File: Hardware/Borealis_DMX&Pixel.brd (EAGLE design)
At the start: 62.5 x 28.3 mm, 9 parts, among them IC2 SP3485, J1 RJ45-854602-908LF

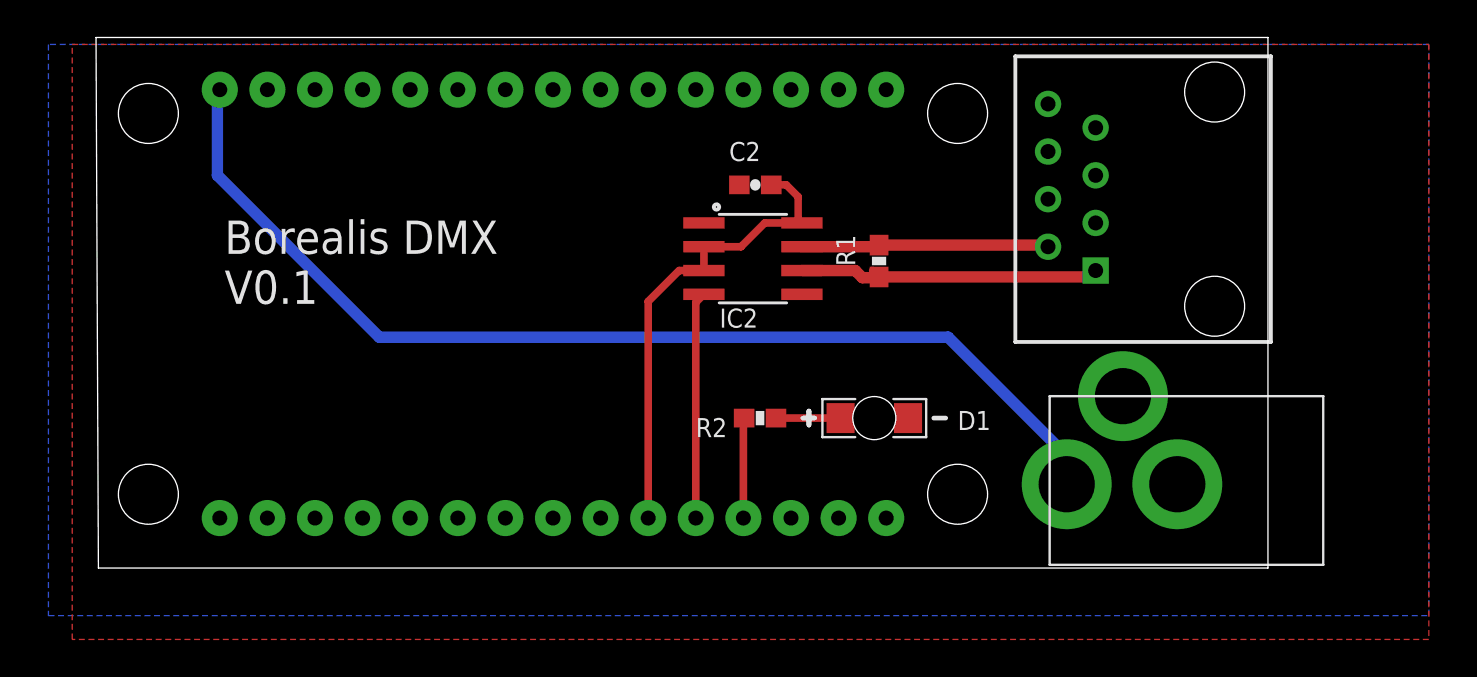
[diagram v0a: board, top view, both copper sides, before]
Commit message: Replaced erroneously committed DMX only output design files with DMX & Pixel version refrenced in repo documentation.
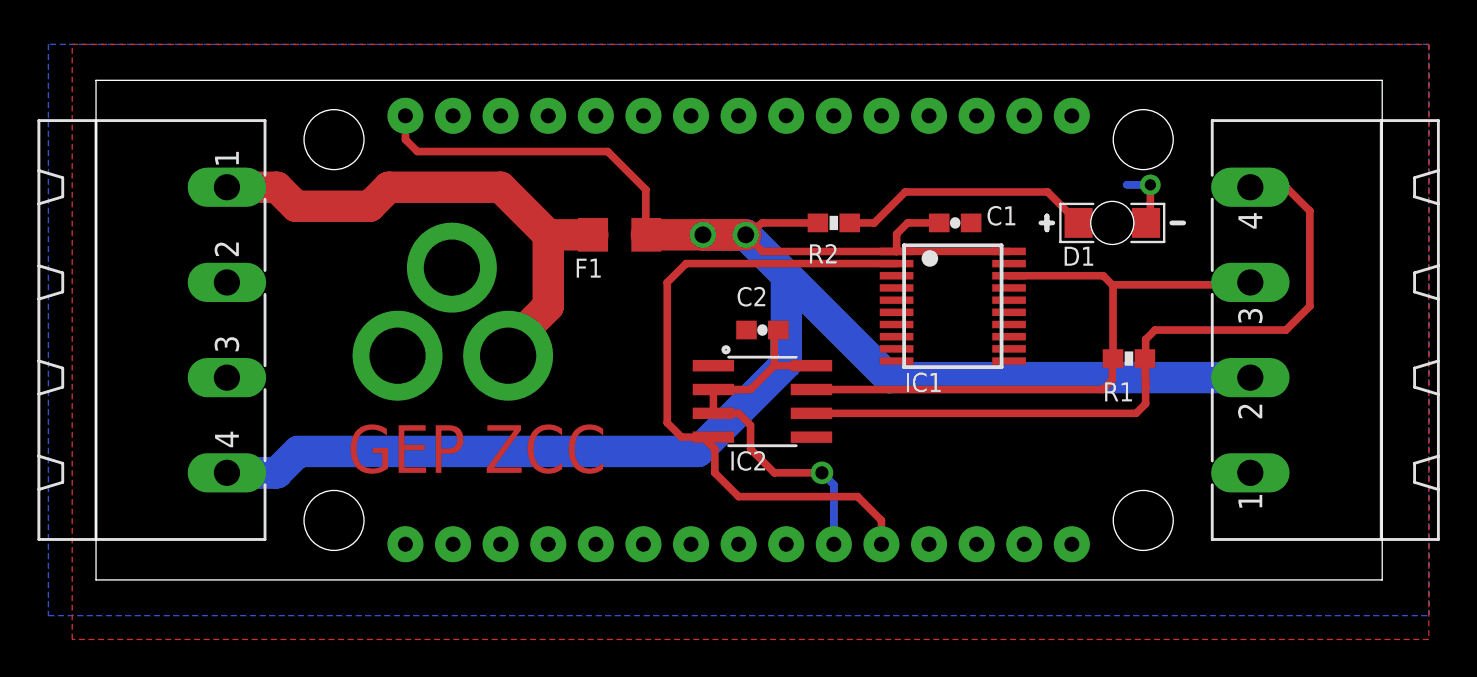
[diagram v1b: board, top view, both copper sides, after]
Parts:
- removed J1: RJ45-854602-908LF, SparkFun-Connectors:RJ45-GREG
- added C1: 1.0uF, SparkFun-Capacitors:0603-CAP
- added F1: 5A 6V, adafruit:R1206
- added IC1: 74245MTC, adafruit:SSOP20
- added INPUT, OUTPUT: MSTBA4, con-phoenix-508:MSTBA4
- R2: value 51 -> (none)
- moved DC_BARRELL_JACK 48.9 mm to (12.7, 12.7), flipped to the bottom
- moved D1 16.4 mm to (54.2, 19.7)
- moved R1 14.3 mm to (55.1, 12.4), turned to 180 degrees
- moved R2 11.1 mm to (39.4, 19.7)
- moved U$1 10.0 mm to (33.0, 14.0)
- moved C2 7.76 mm to (35.6, 14.0)
- moved IC2 7.64 mm to (35.6, 10.2)
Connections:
- removed net DMX-: IC2.7, J1.2, R1.2
- removed net N$1: R2.1, U$1.D3
- new net DATA_OUT/DMX-: IC1.18, IC2.7, OUTPUT.3, R1.2
- new net VCC_RAW: DC_BARRELL_JACK.TIP, F1.1, INPUT.1
- new net VOUT: INPUT.4
- net DATA_UNBUF: now also IC1.2
- net DMX+: now also OUTPUT.4; no longer J1.1
- net GND: now also C1.2, IC1.10, IC1.19, INPUT.2, INPUT.3, OUTPUT.1; no longer J1.7, J1.8
- net VCC: now also C1.1, F1.2, IC1.1, IC1.20, OUTPUT.2, R2.1; no longer DC_BARRELL_JACK.TIP
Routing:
- net VCC: track 57.7 -> 114.5 mm, vias 0 -> 2
- net DATA_OUT/DMX-: track 0.00 -> 34.5 mm
- net VCC_RAW: track 0.00 -> 28.8 mm
- net DMX+: track 16.4 -> 41.3 mm
- net DATA_UNBUF: track 12.1 -> 36.3 mm
- net DMX-: track 13.2 -> 0.00 mm
- net LED_PWR: track 3.45 -> 13.6 mm
- net N$1: track 5.35 -> 0.00 mm
- net 3.3V: track 25.4 -> 20.9 mm, vias 0 -> 1
- net GND: track 0.00 -> 3.86 mm, vias 0 -> 1
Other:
- board size 62.5 x 28.3 mm -> 68.6 x 26.7 mm
- board text added: "Borealis WS2812 / DMX Light Controller"
- board text added: "DMX+"
- board text added: "DMX- / Data"
- board text added: "GEP ZCC"
- board text added: "GND"
- board text added: "PWR"
- board text added: "VIN"
- board text added: "VOUT"
- board text removed: "Activity"
- board text removed: "Borealis DMX V0.1"
